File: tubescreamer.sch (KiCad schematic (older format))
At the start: 0 parts

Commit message: Add schematic files
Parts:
- added C? (x7): C, ~, symbol C
- added C? (x3): CP1, ~, symbol CP1
- added D? (x2): DIODE, ~, symbol DIODE
- added Q? (x2): NPN, ~, symbol NPN
- added R? (x16): R, ~, symbol R
- added RV? (x3): POT, ~, symbol POT
- added U? (x2): TL072, symbol TL072
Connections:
- new net: C?.1, R?.1
- new net: Q?.2 (B), R?.1, R?.2
- new net: C?.1, C?.1, Q?.1 (E), R?.1
- new net: C?.2, R?.1 (x3)
- new net: R?.1, R?.2, U?.3 (+)
- new net: C?.1, C?.1, D?.1 (A), D?.2 (K), R?.1, U?.2 (-)
- new net: C?.2, D?.2 (K), R?.1, RV?.2, U?.1
- new net: R?.2, RV?.1
- new net: C?.1, R?.2, R?.2, RV?.1, U?.3 (+)
- new net: C?.1, R?.2 (x2)
- new net: C?.2, R?.2, U?.1
- new net: R?.1, RV?.3, U?.2 (-)
- new net: C?.1, RV?.2
- new net: R?.1, RV?.1
- new net: C?.2, Q?.2 (B), R?.1
- new net: Q?.1 (E), R?.1, R?.1
- new net +5V: Q?.3 (C), Q?.3 (C), U?.8 (V+), U?.8 (V+)
- new net -5V: C?.2, R?.2, R?.2, R?.2, R?.2, R?.2, U?.4 (V-), U?.4 (V-)
- new net BYPASS_STAGE: RV?.2
- new net FROM_BYPASS: C?.1
- new net GND: R?.1, R?.2, R?.2, R?.2, RV?.3
- new net INPUT: C?.2
- new net OUT: C?.2, R?.1
- new net TO_BYPASS: C?.2

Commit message: Add some values
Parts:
- C?: value C -> 0.02
- C?: value C -> 1 / 50 NP
- C?: value C -> 0.1uF
- C?: value C -> 51pF
- R?: value R -> 1K
- R?: value R -> 520K
- R? (x2): value R -> 10K
- R?: value R -> 51K
- RV?: value POT -> 500KA
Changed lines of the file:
@@
 U 1 1 5511965E
 P 1250 1650
-F 0 "C?" H 1250 1750 40  0000 L CNN
-F 1 "C" H 1256 1565 40  0000 L CNN
+F 0 "C?" V 1350 1750 40  0000 L CNN
+F 1 "0.02" V 1350 1450 40  0000 L CNN
 F 2 "~" H 1288 1500 30  0000 C CNN
 F 3 "~" H 1250 1650 60  0000 C CNN
@@
 P 1850 1650
 F 0 "R?" V 1930 1650 40  0000 C CNN
-F 1 "R" V 1857 1651 40  0000 C CNN
+F 1 "1K" V 1857 1651 40  0000 C CNN
 F 2 "~" V 1780 1650 30  0000 C CNN
 F 3 "~" H 1850 1650 30  0000 C CNN
@@
 U 1 1 5511969B
 P 2200 2000
-F 0 "R?" V 2280 2000 40  0000 C CNN
-F 1 "R" V 2207 2001 40  0000 C CNN
+F 0 "R?" H 2300 1850 40  0000 C CNN
+F 1 "520K" V 2207 2001 40  0000 C CNN
 F 2 "~" V 2130 2000 30  0000 C CNN
 F 3 "~" H 2200 2000 30  0000 C CNN
@@
 U 1 1 551196EC
 P 2900 1950
-F 0 "C?" H 2900 2050 40  0000 L CNN
-F 1 "C" H 2906 1865 40  0000 L CNN
+F 0 "C?" V 2850 2050 40  0000 L CNN
+F 1 "1 / 50 NP" V 3050 1700 40  0000 L CNN
 F 2 "~" H 2938 1800 30  0000 C CNN
 F 3 "~" H 2900 1950 60  0000 C CNN
@@
 U 1 1 551196FB
 P 2900 2200
-F 0 "C?" H 2900 2300 40  0000 L CNN
-F 1 "C" H 2906 2115 40  0000 L CNN
+F 0 "C?" V 2850 2300 40  0000 L CNN
+F 1 "0.1uF" V 2750 2050 40  0000 L CNN
 F 2 "~" H 2938 2050 30  0000 C CNN
 F 3 "~" H 2900 2200 60  0000 C CNN
@@
 U 1 1 5511970A
 P 2650 2550
-F 0 "R?" V 2730 2550 40  0000 C CNN
-F 1 "R" V 2657 2551 40  0000 C CNN
+F 0 "R?" H 2750 2400 40  0000 C CNN
+F 1 "10K" V 2657 2551 40  0000 C CNN
 F 2 "~" V 2580 2550 30  0000 C CNN
 F 3 "~" H 2650 2550 30  0000 C CNN
@@
 U 1 1 55119830
 P 3950 2300
-F 0 "R?" V 4030 2300 40  0000 C CNN
-F 1 "R" V 3957 2301 40  0000 C CNN
+F 0 "R?" H 4050 2100 40  0000 C CNN
+F 1 "10K" V 3957 2301 40  0000 C CNN
 F 2 "~" V 3880 2300 30  0000 C CNN
 F 3 "~" H 3950 2300 30  0000 C CNN
@@
 U 1 1 5511983F
 P 4850 3050
-F 0 "D?" H 4850 3150 40  0000 C CNN
-F 1 "DIODE" H 4850 2950 40  0000 C CNN
+F 0 "D?" H 4650 3100 40  0000 C CNN
+F 1 "DIODE" H 5050 2950 40  0000 C CNN
 F 2 "~" H 4850 3050 60  0000 C CNN
 F 3 "~" H 4850 3050 60  0000 C CNN
@@
 U 1 1 55119856
 P 4850 3300
-F 0 "D?" H 4850 3400 40  0000 C CNN
-F 1 "DIODE" H 4850 3200 40  0000 C CNN
+F 0 "D?" H 4700 3350 40  0000 C CNN
+F 1 "DIODE" H 5050 3250 40  0000 C CNN
 F 2 "~" H 4850 3300 60  0000 C CNN
 F 3 "~" H 4850 3300 60  0000 C CNN
@@
 U 1 1 551198CB
 P 4850 2800
-F 0 "C?" H 4850 2900 40  0000 L CNN
-F 1 "C" H 4856 2715 40  0000 L CNN
+F 0 "C?" V 4900 2950 40  0000 L CNN
+F 1 "51pF" V 4900 2600 40  0000 L CNN
 F 2 "~" H 4888 2650 30  0000 C CNN
 F 3 "~" H 4850 2800 60  0000 C CNN
@@
 U 1 1 551198F8
 P 4250 3700
-F 0 "R?" V 4330 3700 40  0000 C CNN
-F 1 "R" V 4257 3701 40  0000 C CNN
+F 0 "R?" H 4350 3550 40  0000 C CNN
+F 1 "51K" V 4257 3701 40  0000 C CNN
 F 2 "~" V 4180 3700 30  0000 C CNN
 F 3 "~" H 4250 3700 30  0000 C CNN
@@
 P 4800 3950
 F 0 "RV?" H 4800 3850 50  0000 C CNN
-F 1 "POT" H 4800 3950 50  0000 C CNN
+F 1 "500KA" H 4800 3950 50  0000 C CNN
 F 2 "~" H 4800 3950 60  0000 C CNN
 F 3 "~" H 4800 3950 60  0000 C CNN

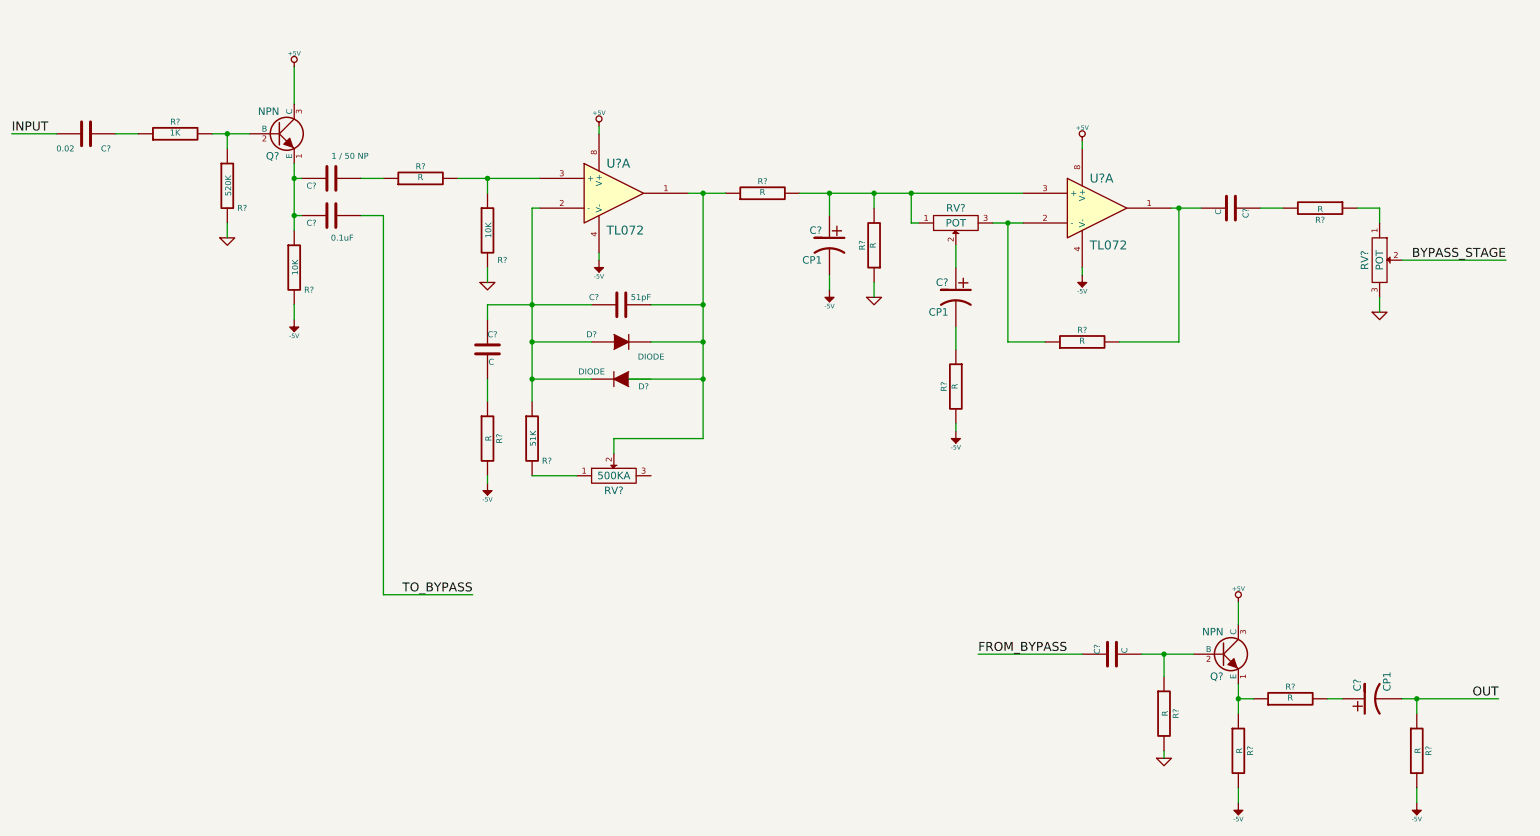
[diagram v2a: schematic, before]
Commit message: colocados los valores de los componentes
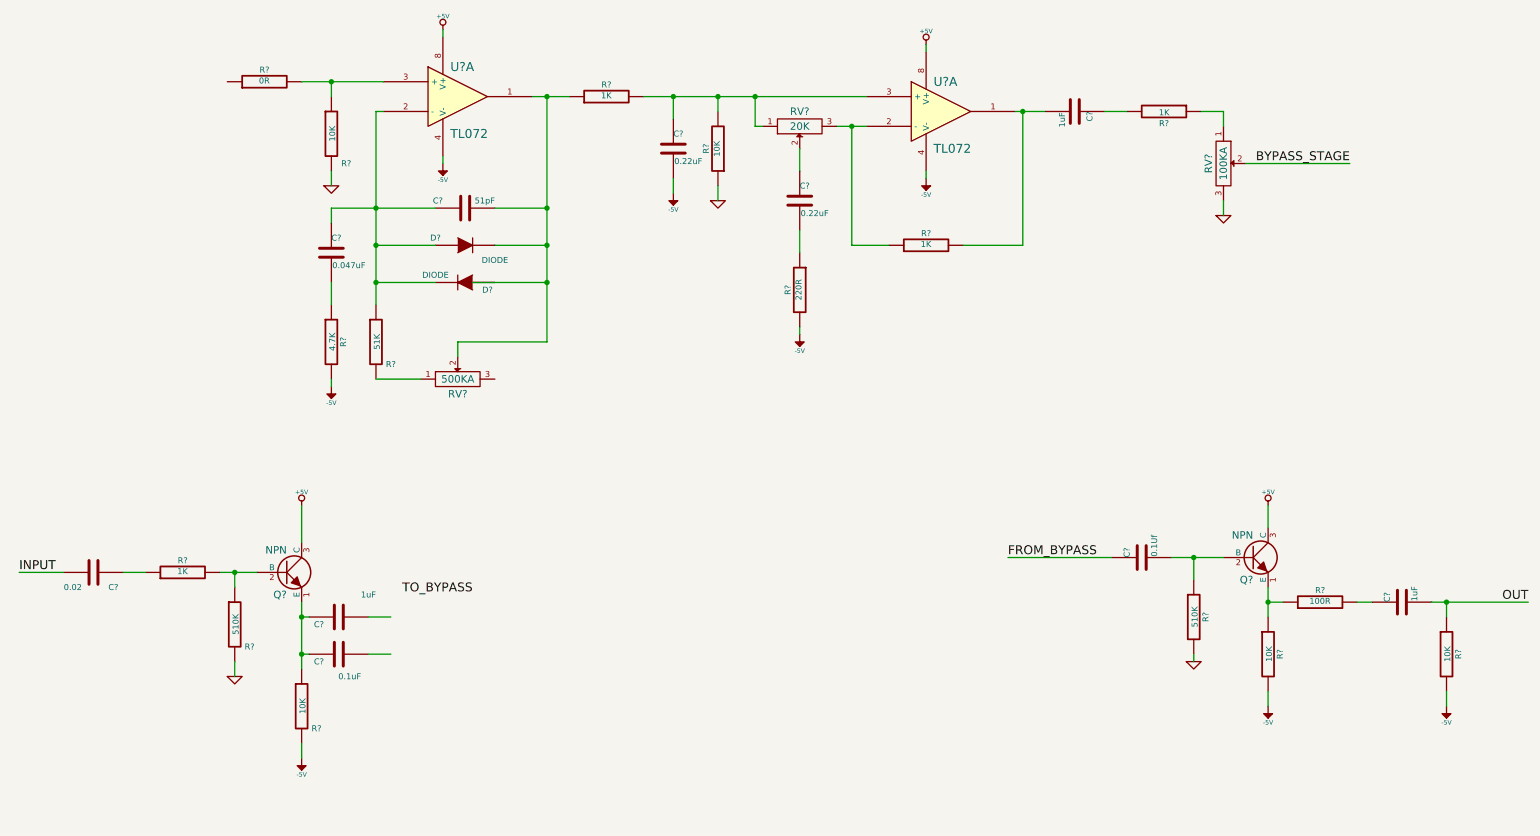
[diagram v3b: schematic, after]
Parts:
- removed C? (x3): CP1, ~, symbol CP1
- added C? (x2): 0.22uF, ~, symbol C
- added C?: 1uF, ~, symbol C
- C?: value 1 / 50 NP -> 1uF
- C?: value C -> 0.047uF
- C?: value C -> 1uF
- C?: value C -> 0.1Uf
- R?: value 520K -> 510K
- R?: value R -> 0R
- R?: value R -> 4.7K
- R? (x3): value R -> 1K
- R? (x3): value R -> 10K
- R?: value R -> 220R
- R?: value R -> 510K
- R?: value R -> 100R
- RV?: value POT -> 20K
- RV?: value POT -> 100KA
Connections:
- wire segments 70 -> 68
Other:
- moved on the sheet: C?, D?, Q?, R?, RV?, U?A
